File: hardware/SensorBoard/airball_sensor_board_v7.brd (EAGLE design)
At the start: 139.7 x 38.1 mm, 27 parts, among them J1 FEMALE 2x3

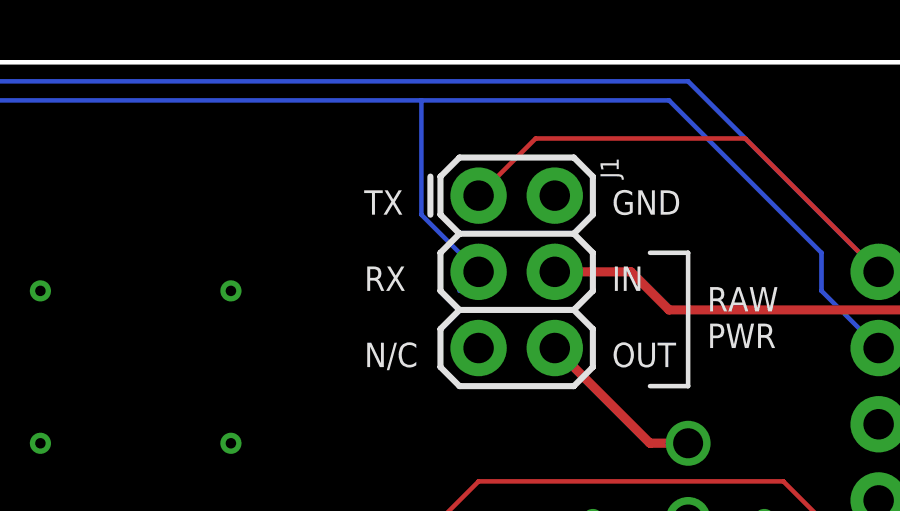
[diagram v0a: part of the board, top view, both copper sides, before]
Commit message: Minor fix to remove an airwire.
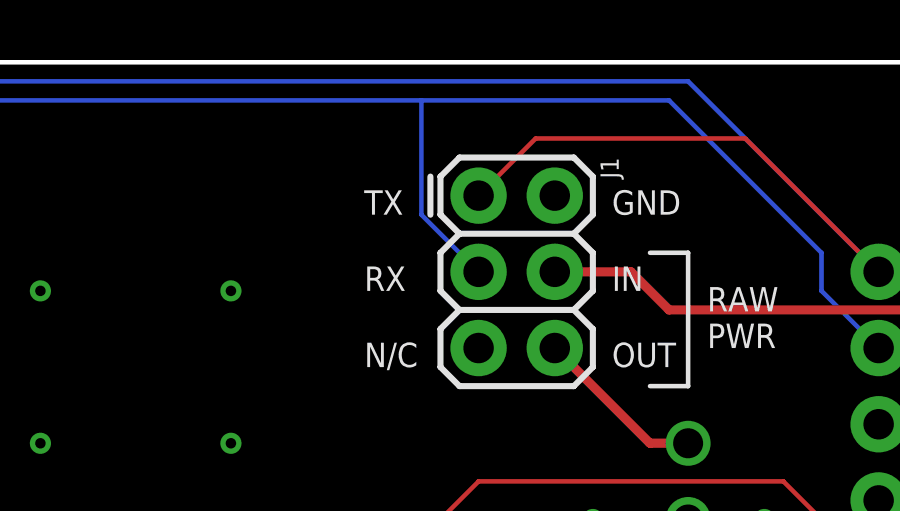
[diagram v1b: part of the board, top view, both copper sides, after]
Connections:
- net N$1 renamed BATT_REGULATOR_OUTPUT
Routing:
- net ARDUINO_RX: track 118.9 -> 117.6 mm
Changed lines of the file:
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@@
 <grid distance="25" unitdist="mil" unit="mil" style="lines" multiple="1" display="yes" altdistance="5" altunitdist="mil" altunit="mil"/>
 <layers>
-<layer number="1" name="Top" color="4" fill="1" visible="yes" active="yes"/>
+<layer number="1" name="Top" color="4" fill="1" visible="no" active="yes"/>
 <layer number="2" name="Route2" color="1" fill="3" visible="no" active="no"/>
 <layer number="3" name="Route3" color="4" fill="3" visible="no" active="no"/>
@@
 <layer number="14" name="Route14" color="1" fill="6" visible="no" active="no"/>
 <layer number="15" name="Route15" color="4" fill="6" visible="no" active="no"/>
-<layer number="16" name="Bottom" color="1" fill="1" visible="no" active="yes"/>
+<layer number="16" name="Bottom" color="1" fill="1" visible="yes" active="yes"/>
 <layer number="17" name="Pads" color="2" fill="1" visible="yes" active="yes"/>
 <layer number="18" name="Vias" color="2" fill="1" visible="yes" active="yes"/>
 <layer number="19" name="Unrouted" color="6" fill="1" visible="yes" active="yes"/>
 <layer number="20" name="Dimension" color="15" fill="1" visible="yes" active="yes"/>
-<layer number="21" name="tPlace" color="7" fill="1" visible="yes" active="yes"/>
-<layer number="22" name="bPlace" color="7" fill="1" visible="no" active="yes"/>
-<layer number="23" name="tOrigins" color="15" fill="1" visible="yes" active="yes"/>
-<layer number="24" name="bOrigins" color="15" fill="1" visible="no" active="yes"/>
-<layer number="25" name="tNames" color="7" fill="1" visible="yes" active="yes"/>
-<layer number="26" name="bNames" color="7" fill="1" visible="no" active="yes"/>
+<layer number="21" name="tPlace" color="7" fill="1" visible="no" active="yes"/>
+<layer number="22" name="bPlace" color="7" fill="1" visible="yes" active="yes"/>
+<layer number="23" name="tOrigins" color="15" fill="1" visible="no" active="yes"/>
+<layer number="24" name="bOrigins" color="15" fill="1" visible="yes" active="yes"/>
+<layer number="25" name="tNames" color="7" fill="1" visible="no" active="yes"/>
+<layer number="26" name="bNames" color="7" fill="1" visible="yes" active="yes"/>
 <layer number="27" name="tValues" color="7" fill="1" visible="no" active="yes"/>
 <layer number="28" name="bValues" color="7" fill="1" visible="no" active="yes"/>
@@
 <layer number="37" name="tTest" color="7" fill="1" visible="no" active="yes"/>
 <layer number="38" name="bTest" color="7" fill="1" visible="no" active="yes"/>
-<layer number="39" name="tKeepout" color="4" fill="11" visible="yes" active="yes"/>
-<layer number="40" name="bKeepout" color="1" fill="11" visible="no" active="yes"/>
-<layer number="41" name="tRestrict" color="4" fill="10" visible="yes" active="yes"/>
-<layer number="42" name="bRestrict" color="1" fill="10" visible="no" active="yes"/>
+<layer number="39" name="tKeepout" color="4" fill="11" visible="no" active="yes"/>
+<layer number="40" name="bKeepout" color="1" fill="11" visible="yes" active="yes"/>
+<layer number="41" name="tRestrict" color="4" fill="10" visible="no" active="yes"/>
+<layer number="42" name="bRestrict" color="1" fill="10" visible="yes" active="yes"/>
 <layer number="43" name="vRestrict" color="2" fill="10" visible="no" active="yes"/>
 <layer number="44" name="Drills" color="7" fill="1" visible="no" active="yes"/>
@@
 <layer number="49" name="Reference" color="7" fill="1" visible="no" active="yes"/>
 <layer number="50" name="dxf" color="7" fill="1" visible="no" active="no"/>
-<layer number="51" name="tDocu" color="7" fill="1" visible="yes" active="yes"/>
-<layer number="52" name="bDocu" color="7" fill="1" visible="no" active="yes"/>
+<layer number="51" name="tDocu" color="7" fill="1" visible="no" active="yes"/>
+<layer number="52" name="bDocu" color="7" fill="1" visible="yes" active="yes"/>
 <layer number="53" name="tGND_GNDA" color="7" fill="9" visible="no" active="no"/>
 <layer number="54" name="bGND_GNDA" color="1" fill="9" visible="no" active="no"/>
@@
 <wire x1="31.765" y1="9.445" x2="31.765" y2="29.225" width="0.1524" layer="16"/>
 <contactref element="J1" pad="3"/>
-<wire x1="100.33" y1="31.75" x2="100.33" y2="30.48" width="0.1524" layer="16"/>
-<wire x1="100.965" y1="31.115" x2="99.06" y2="33.02" width="0.1524" layer="16"/>
-<wire x1="99.06" y1="33.02" x2="99.06" y2="36.83" width="0.1524" layer="16"/>
+<wire x1="99.06" y1="36.83" x2="99.06" y2="33.02" width="0.1524" layer="16"/>
 <wire x1="112.395" y1="30.48" x2="114.3" y2="28.575" width="0.1524" layer="16"/>
 <wire x1="107.315" y1="36.83" x2="112.395" y2="31.75" width="0.1524" layer="16"/>
 <wire x1="112.395" y1="31.75" x2="112.395" y2="30.48" width="0.1524" layer="16"/>
 <wire x1="99.06" y1="36.83" x2="107.315" y2="36.83" width="0.1524" layer="16"/>
-<wire x1="100.965" y1="31.115" x2="100.33" y2="31.75" width="0" layer="19" extent="16-16"/>
+<wire x1="99.06" y1="33.02" x2="100.965" y2="31.115" width="0.1524" layer="16"/>
 </signal>
 <signal name="V_BATT_SWITCHED">
@@
 <wire x1="99.44236875" y1="7.9375" x2="93.0275" y2="7.9375" width="0.1524" layer="16"/>
 </signal>
-<signal name="N$1">
+<signal name="BATT_REGULATOR_OUTPUT">
 <contactref element="U$1" pad="P$5"/>
 <contactref element="J1" pad="6"/>

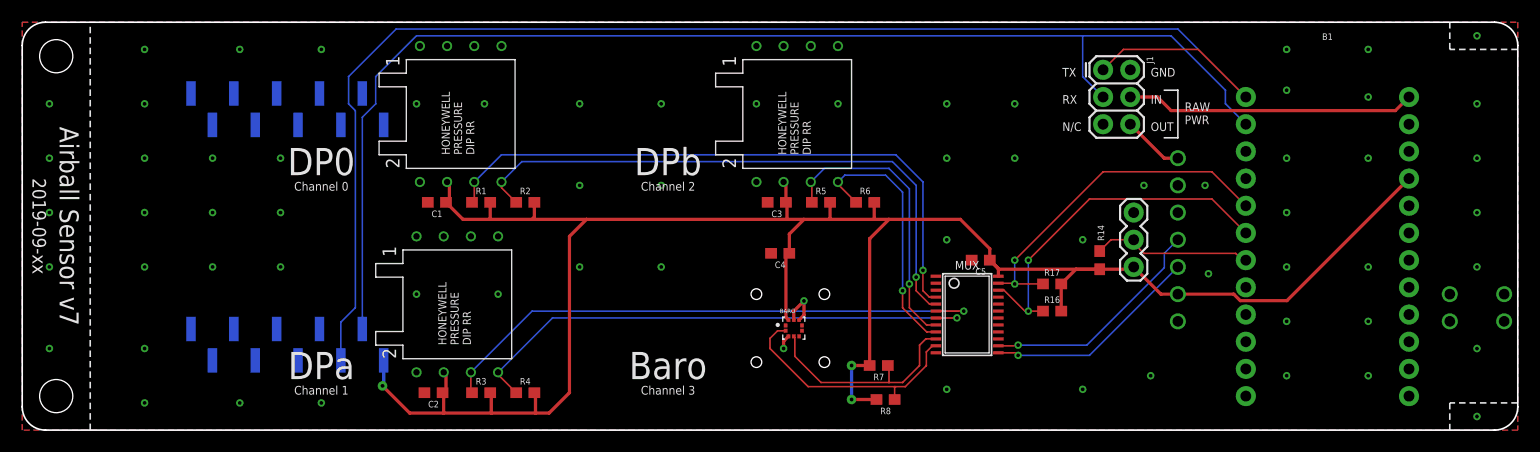
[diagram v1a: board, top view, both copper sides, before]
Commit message: Improved routing of UART traces - added a ground plane between them and moved them away from board edge.
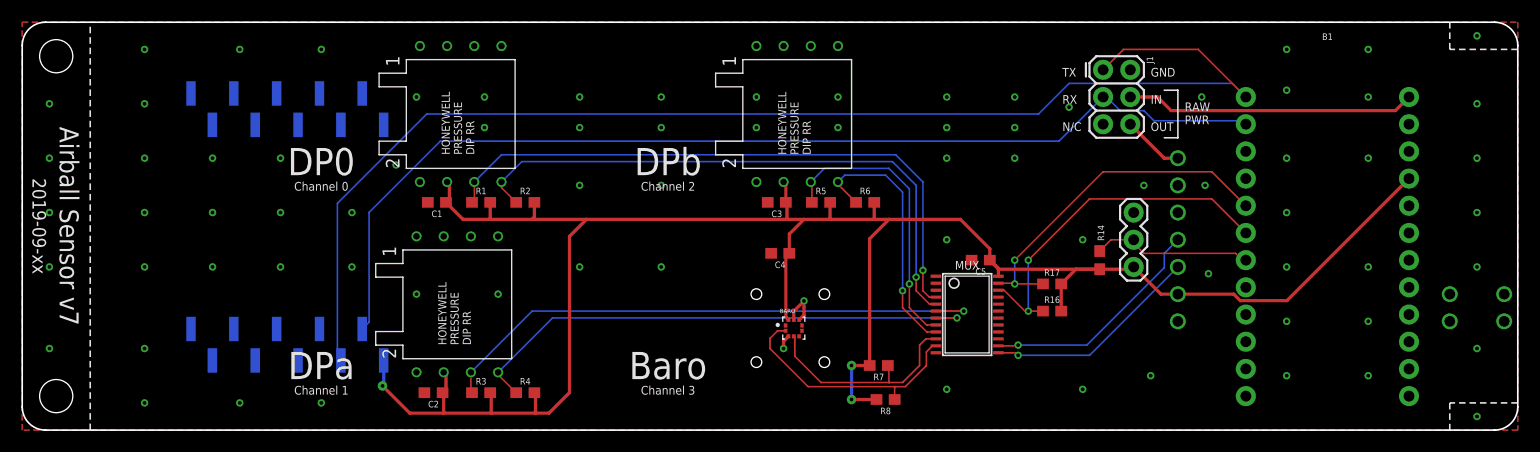
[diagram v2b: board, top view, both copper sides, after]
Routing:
- net ARDUINO_RX: track 117.6 -> 98.6 mm
- net ARDUINO_TX: track 131.6 -> 120.8 mm
- net GND: vias 6 -> 8
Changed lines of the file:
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@@
 <setting verticaltext="up"/>
 </settings>
-<grid distance="25" unitdist="mil" unit="mil" style="lines" multiple="1" display="yes" altdistance="5" altunitdist="mil" altunit="mil"/>
+<grid distance="12.5" unitdist="mil" unit="mil" style="lines" multiple="1" display="yes" altdistance="5" altunitdist="mil" altunit="mil"/>
 <layers>
-<layer number="1" name="Top" color="4" fill="1" visible="no" active="yes"/>
+<layer number="1" name="Top" color="4" fill="1" visible="yes" active="yes"/>
 <layer number="2" name="Route2" color="1" fill="3" visible="no" active="no"/>
 <layer number="3" name="Route3" color="4" fill="3" visible="no" active="no"/>
@@
 <layer number="19" name="Unrouted" color="6" fill="1" visible="yes" active="yes"/>
 <layer number="20" name="Dimension" color="15" fill="1" visible="yes" active="yes"/>
-<layer number="21" name="tPlace" color="7" fill="1" visible="no" active="yes"/>
+<layer number="21" name="tPlace" color="7" fill="1" visible="yes" active="yes"/>
 <layer number="22" name="bPlace" color="7" fill="1" visible="yes" active="yes"/>
-<layer number="23" name="tOrigins" color="15" fill="1" visible="no" active="yes"/>
+<layer number="23" name="tOrigins" color="15" fill="1" visible="yes" active="yes"/>
 <layer number="24" name="bOrigins" color="15" fill="1" visible="yes" active="yes"/>
-<layer number="25" name="tNames" color="7" fill="1" visible="no" active="yes"/>
+<layer number="25" name="tNames" color="7" fill="1" visible="yes" active="yes"/>
 <layer number="26" name="bNames" color="7" fill="1" visible="yes" active="yes"/>
 <layer number="27" name="tValues" color="7" fill="1" visible="no" active="yes"/>
@@
 <layer number="37" name="tTest" color="7" fill="1" visible="no" active="yes"/>
 <layer number="38" name="bTest" color="7" fill="1" visible="no" active="yes"/>
-<layer number="39" name="tKeepout" color="4" fill="11" visible="no" active="yes"/>
+<layer number="39" name="tKeepout" color="4" fill="11" visible="yes" active="yes"/>
 <layer number="40" name="bKeepout" color="1" fill="11" visible="yes" active="yes"/>
-<layer number="41" name="tRestrict" color="4" fill="10" visible="no" active="yes"/>
+<layer number="41" name="tRestrict" color="4" fill="10" visible="yes" active="yes"/>
 <layer number="42" name="bRestrict" color="1" fill="10" visible="yes" active="yes"/>
 <layer number="43" name="vRestrict" color="2" fill="10" visible="no" active="yes"/>
@@
 <layer number="49" name="Reference" color="7" fill="1" visible="no" active="yes"/>
 <layer number="50" name="dxf" color="7" fill="1" visible="no" active="no"/>
-<layer number="51" name="tDocu" color="7" fill="1" visible="no" active="yes"/>
+<layer number="51" name="tDocu" color="7" fill="1" visible="yes" active="yes"/>
 <layer number="52" name="bDocu" color="7" fill="1" visible="yes" active="yes"/>
 <layer number="53" name="tGND_GNDA" color="7" fill="9" visible="no" active="no"/>
@@
 <via x="135.89" y="36.83" extent="1-16" drill="0.35"/>
 <contactref element="J1" pad="2"/>
+<via x="97.79" y="30.1625" extent="1-16" drill="0.35"/>
+<via x="110.1725" y="31.115" extent="1-16" drill="0.35"/>
 </signal>
 <signal name="MUX_SDA">
@@
 <contactref element="B1" pad="1"/>
 <contactref element="XBEE" pad="3"/>
-<wire x1="114.3" y1="31.115" x2="107.95" y2="37.465" width="0.1524" layer="16"/>
-<wire x1="34.925" y1="37.465" x2="107.95" y2="37.465" width="0.1524" layer="16"/>
-<wire x1="34.925" y1="37.465" x2="30.48" y2="33.02" width="0.1524" layer="16"/>
-<wire x1="30.48" y1="33.02" x2="30.48" y2="30.48" width="0.1524" layer="16"/>
-<wire x1="30.48" y1="30.48" x2="31.115" y2="29.845" width="0.1524" layer="16"/>
-<wire x1="31.115" y1="29.845" x2="31.115" y2="11.43" width="0.1524" layer="16"/>
-<wire x1="29.765" y1="10.08" x2="29.765" y2="6.51" width="0.1524" layer="16"/>
-<wire x1="31.115" y1="11.43" x2="29.765" y2="10.08" width="0.1524" layer="16"/>
+<wire x1="114.3" y1="31.115" x2="113.03" y2="32.385" width="0.1524" layer="16"/>
+<wire x1="113.03" y1="32.385" x2="97.79" y2="32.385" width="0.1524" layer="16"/>
 <contactref element="J1" pad="1"/>
 <wire x1="114.3" y1="31.115" x2="109.855" y2="35.56" width="0.1524" layer="1"/>
 <wire x1="109.855" y1="35.56" x2="102.87" y2="35.56" width="0.1524" layer="1"/>
 <wire x1="102.87" y1="35.56" x2="100.965" y2="33.655" width="0.1524" layer="1"/>
+<wire x1="97.79" y1="32.385" x2="94.9325" y2="29.5275" width="0.1524" layer="16"/>
+<wire x1="94.9325" y1="29.5275" x2="37.7825" y2="29.5275" width="0.1524" layer="16"/>
+<wire x1="29.4475" y1="21.1925" x2="29.4475" y2="6.8275" width="0.1524" layer="16"/>
+<wire x1="29.4475" y1="6.8275" x2="29.765" y2="6.51" width="0.1524" layer="16"/>
+<wire x1="37.7825" y1="29.5275" x2="29.4475" y2="21.1925" width="0.1524" layer="16"/>
 </signal>
 <signal name="ARDUINO_RX">
 <contactref element="B1" pad="2"/>
 <contactref element="XBEE" pad="2"/>
-<wire x1="99.06" y1="36.83" x2="36.83" y2="36.83" width="0.1524" layer="16"/>
-<wire x1="36.83" y1="36.83" x2="33.02" y2="33.02" width="0.1524" layer="16"/>
-<wire x1="33.02" y1="33.02" x2="33.02" y2="30.48" width="0.1524" layer="16"/>
-<wire x1="33.02" y1="30.48" x2="31.765" y2="29.225" width="0.1524" layer="16"/>
-<wire x1="31.765" y1="9.445" x2="31.765" y2="29.225" width="0.1524" layer="16"/>
+<wire x1="100.965" y1="31.115" x2="96.8375" y2="26.9875" width="0.1524" layer="16"/>
+<wire x1="96.8375" y1="26.9875" x2="39.0525" y2="26.9875" width="0.1524" layer="16"/>
 <contactref element="J1" pad="3"/>
-<wire x1="99.06" y1="36.83" x2="99.06" y2="33.02" width="0.1524" layer="16"/>
-<wire x1="112.395" y1="30.48" x2="114.3" y2="28.575" width="0.1524" layer="16"/>
-<wire x1="107.315" y1="36.83" x2="112.395" y2="31.75" width="0.1524" layer="16"/>
-<wire x1="112.395" y1="31.75" x2="112.395" y2="30.48" width="0.1524" layer="16"/>
-<wire x1="99.06" y1="36.83" x2="107.315" y2="36.83" width="0.1524" layer="16"/>
-<wire x1="99.06" y1="33.02" x2="100.965" y2="31.115" width="0.1524" layer="16"/>
+<wire x1="100.965" y1="31.115" x2="101.2825" y2="31.115" width="0.1524" layer="16"/>
+<wire x1="101.2825" y1="31.115" x2="102.5525" y2="29.845" width="0.1524" layer="16"/>
+<wire x1="113.9825" y1="28.8925" x2="114.3" y2="28.575" width="0.1524" layer="16"/>
+<wire x1="105.7275" y1="28.8925" x2="113.9825" y2="28.8925" width="0.1524" layer="16"/>
+<wire x1="39.0525" y1="26.9875" x2="32.4" y2="20.335" width="0.1524" layer="16"/>
+<wire x1="32.4" y1="20.335" x2="32.4" y2="10.08" width="0.1524" layer="16"/>
+<wire x1="32.4" y1="10.08" x2="31.765" y2="9.445" width="0.1524" layer="16"/>
+<wire x1="102.5525" y1="29.845" x2="104.775" y2="29.845" width="0.1524" layer="16"/>
+<wire x1="104.775" y1="29.845" x2="105.7275" y2="28.8925" width="0.1524" layer="16"/>
 </signal>
 <signal name="V_BATT_SWITCHED">
@@
 </signal>
 <signal name="GND20" class="1">
-<via x="92.71" y="30.48" extent="1-16" drill="0.35"/>
+<via x="92.71" y="31.115" extent="1-16" drill="0.35"/>
 </signal>
 <signal name="GND21" class="1">
-<via x="86.36" y="30.48" extent="1-16" drill="0.35"/>
+<via x="86.36" y="31.115" extent="1-16" drill="0.35"/>
 </signal>
 <signal name="GND22" class="1">
@@
 </signal>
 <signal name="GND29" class="1">
-<via x="76.2" y="30.48" extent="1-16" drill="0.35"/>
+<via x="76.2" y="31.115" extent="1-16" drill="0.35"/>
 </signal>
 <signal name="GND30" class="1">
-<via x="68.58" y="30.48" extent="1-16" drill="0.35"/>
+<via x="68.58" y="31.115" extent="1-16" drill="0.35"/>
 </signal>
 <signal name="GND31" class="1">
-<via x="43.18" y="30.48" extent="1-16" drill="0.35"/>
+<via x="43.18" y="31.115" extent="1-16" drill="0.35"/>
 </signal>
 <signal name="GND32" class="1">
-<via x="36.83" y="30.48" extent="1-16" drill="0.35"/>
+<via x="36.83" y="31.115" extent="1-16" drill="0.35"/>
 </signal>
 <signal name="GND33" class="1">
@@
 </signal>
 <signal name="GND35" class="1">
-<via x="59.69" y="30.48" extent="1-16" drill="0.35"/>
+<via x="59.69" y="31.115" extent="1-16" drill="0.35"/>
 </signal>
 <signal name="GND36" class="1">
-<via x="52.07" y="30.48" extent="1-16" drill="0.35"/>
+<via x="52.07" y="31.115" extent="1-16" drill="0.35"/>
 </signal>
 <signal name="GND37" class="1">
@@
 <via x="24.13" y="15.24" extent="1-16" drill="0.35"/>
 </signal>
+<signal name="GND64" class="1">
+<via x="86.36" y="28.2575" extent="1-16" drill="0.35"/>
+</signal>
+<signal name="GND65" class="1">
+<via x="92.71" y="28.2575" extent="1-16" drill="0.35"/>
+</signal>
+<signal name="GND66" class="1">
+<via x="76.2" y="28.2575" extent="1-16" drill="0.35"/>
+</signal>
+<signal name="GND67" class="1">
+<via x="68.58" y="28.2575" extent="1-16" drill="0.35"/>
+</signal>
+<signal name="GND68" class="1">
+<via x="59.69" y="28.2575" extent="1-16" drill="0.35"/>
+</signal>
+<signal name="GND69" class="1">
+<via x="52.07" y="28.2575" extent="1-16" drill="0.35"/>
+</signal>
+<signal name="GND70" class="1">
+<via x="43.18" y="28.2575" extent="1-16" drill="0.35"/>
+</signal>
+<signal name="GND71" class="1">
+<via x="30.7975" y="20.32" extent="1-16" drill="0.35"/>
+</signal>
+<signal name="GND72" class="1">
+<via x="30.7975" y="15.24" extent="1-16" drill="0.35"/>
+</signal>
+<signal name="GND73" class="1">
+<via x="34.925" y="24.765" extent="1-16" drill="0.35"/>
+</signal>
 </signals>
